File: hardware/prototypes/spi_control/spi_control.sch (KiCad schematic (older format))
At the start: 78 parts, among them J1 USB_B_Micro, J39 Versa_1, J40 Versa_2, U1 ST1L08SPU33R, U2 MCP2210-I_MQ, U3 ADAR7251, U4 BGT24_Module, Y1 12MHZ, Y2 40MHz

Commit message: Started routing SPI to USB. Started preliminary routing for the IQ data.
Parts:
- removed Y1: 12MHZ, Crystal:Crystal_SMD_Abracon_ABM8G-4Pin_3.2x2.5mm, symbol Device:Crystal
- removed Y2: 40MHz, Oscillator:Oscillator_SMD_Abracon_ASE-4Pin_3.2x2.5mm, symbol Device:Crystal
- added Y1: 12MHZ, Crystal:Crystal_SMD_Abracon_ABM8G-4Pin_3.2x2.5mm, symbol Device:Crystal_GND24
- added Y2: 40MHz, Oscillator:Oscillator_SMD_Abracon_ASE-4Pin_3.2x2.5mm, symbol Device:Crystal_GND24
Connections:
- net GND: now also Y1.2, Y1.4, Y2.2, Y2.4
- net PLL_MOD: now also J40.21 (Pin_21); no longer J40.25 (Pin_25)
- net PLL_RSET: now also J40.25 (Pin_25); no longer J40.21 (Pin_21)
- net USB_D+: now also D1.4; no longer D1.3
- net USB_D-: now also D1.3; no longer D1.4
- net at C21.2, U2.19 (OSC1): now also Y1.1
- net at C23.2, U2.20 (OSC2): now also Y1.3
- net at C26.2, R7.1: now also Y2.1
- net at C25.2, R6.1: now also Y2.3
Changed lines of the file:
@@
 $EndComp
 Wire Wire Line
-	1450 1500 1850 1500
-Wire Wire Line
-	2050 2000 1950 2000
-Wire Wire Line
-	1950 2000 1950 1600
-Wire Wire Line
 	1950 1600 1450 1600
 Wire Wire Line
-	2050 2200 1850 2200
-Wire Wire Line
-	1850 2200 1850 1500
-Wire Wire Line
 	2550 2000 2650 2000
 Wire Wire Line
@@
 Wire Wire Line
 	2850 2500 2850 2550
-$Comp
-L Device:Crystal Y1
-U 1 1 5DA6AEC7
-P 7500 2500
-F 0 "Y1" H 7500 2750 50  0000 C CNN
-F 1 "12MHZ" H 7500 2677 50  0000 C CNN
-F 2 "Crystal:Crystal_SMD_Abracon_ABM8G-4Pin_3.2x2.5mm" H 7500 2500 50  0001 C CNN
-F 3 "https://ecsxtal.com/store/pdf/ecx-32.pdf" H 7500 2500 50  0001 C CNN
-F 4 "ECS-120-12-33-AGN-TR" H 7500 2676 50  0001 C CNN "MPN"
-	1    7500 2500
-	1    0    0    -1
-$EndComp
 Wire Wire Line
 	7750 2250 7750 2500
@@
 	7250 2900 7250 2950
 Wire Wire Line
-	7250 2950 7500 2950
-Wire Wire Line
 	7750 2950 7750 2900
 $Comp
@@
 PLL Loop Filter
 $Comp
-L Device:Crystal Y2
-U 1 1 5DD040BC
-P 10700 8850
-F 0 "Y2" V 10746 8981 50  0000 L CNN
-F 1 "40MHz" V 10655 8981 50  0000 L CNN
-F 2 "Oscillator:Oscillator_SMD_Abracon_ASE-4Pin_3.2x2.5mm" H 10700 8850 50  0001 C CNN
-F 3 "https://ecsxtal.com/store/pdf/ecx-32.pdf" H 10700 8850 50  0001 C CNN
-F 4 "ECS-400-18-33-JGN-TR" V 10700 8850 50  0001 C CNN "MPN"
-	1    10700 8850
-	0    -1   -1   0
-$EndComp
-$Comp
 L Device:C C25
 U 1 1 5DD05357
@@
 $EndComp
 Wire Wire Line
-	10350 8600 10700 8600
-Wire Wire Line
-	10700 8700 10700 8600
-Connection ~ 10700 8600
-Wire Wire Line
-	10700 8600 10900 8600
-Wire Wire Line
 	11200 8600 11250 8600
 Wire Wire Line
@@
 	10900 9100 10700 9100
 Wire Wire Line
-	10700 9100 10700 9000
-Wire Wire Line
 	10700 9100 10350 9100
 Connection ~ 10700 9100
@@
 PLL_TRIG2
 Wire Wire Line
-	19250 5450 19250 6100
-Text Label 19250 6100 1    50   ~ 0
+	19050 5450 19050 6100
+Text Label 19050 6100 1    50   ~ 0
 PLL_MOD
 Wire Wire Line
@@
 PLL_MUX
 Wire Wire Line
-	19050 5450 19050 6100
-Text Label 19050 6100 1    50   ~ 0
+	19250 5450 19250 6100
+Text Label 19250 6100 1    50   ~ 0
 PLL_RSET
 Wire Wire Line
@@
 EndData
 $EndBitmap
+Wire Wire Line
+	1950 1600 1950 2200
+Wire Wire Line
+	1950 2200 2050 2200
+Wire Wire Line
+	2050 2000 2050 1500
+Wire Wire Line
+	1450 1500 2050 1500
+$Comp
+L Device:Crystal_GND24 Y1
+U 1 1 5FC6E4E6
+P 7500 2500
+F 0 "Y1" H 7694 2546 50  0000 L CNN
+F 1 "12MHZ" H 7375 2750 50  0000 L CNN
+F 2 "Crystal:Crystal_SMD_Abracon_ABM8G-4Pin_3.2x2.5mm" H 7500 2500 50  0001 C CNN
+F 3 "https://ecsxtal.com/store/pdf/ecx-32.pdf" H 7500 2500 50  0001 C CNN
+F 4 "ECS-120-12-33-AGN-TR" H 7500 2500 50  0001 C CNN "MPN"
+	1    7500 2500
+	1    0    0    -1
+$EndComp
+Connection ~ 10700 8600
+Wire Wire Line
+	10700 8600 10900 8600
+Wire Wire Line
+	10350 8600 10700 8600
+Wire Wire Line
+	10700 8600 10700 8725
+Wire Wire Line
+	10700 9100 10700 9025
+Wire Wire Line
+	7250 2950 7500 2950
+Wire Wire Line
+	7500 2950 7500 2700
+Wire Wire Line
+	7500 2300 7500 2200
+Wire Wire Line
+	7500 2200 7675 2200
+$Comp
+L power:GND #PWR0146
+U 1 1 60004941
+P 7675 2350
+F 0 "#PWR0146" H 7675 2100 50  0001 C CNN
+F 1 "GND" H 7600 2375 50  0000 C CNN
+F 2 "" H 7675 2350 50  0001 C CNN
+F 3 "" H 7675 2350 50  0001 C CNN
+	1    7675 2350
+	1    0    0    -1
+$EndComp
+Wire Wire Line
+	7675 2200 7675 2350
+$Comp
+L power:GND #PWR0147
+U 1 1 600397BF
+P 10950 8875
+F 0 "#PWR0147" H 10950 8625 50  0001 C CNN
+F 1 "GND" H 10955 8702 50  0000 C CNN
+F 2 "" H 10950 8875 50  0001 C CNN
+F 3 "" H 10950 8875 50  0001 C CNN
+	1    10950 8875
+	1    0    0    -1
+$EndComp
+$Comp
+L Device:Crystal_GND24 Y2
+U 1 1 5FD6D80E
+P 10700 8875
+F 0 "Y2" H 10850 9125 50  0000 L CNN
+F 1 "40MHz" H 10575 9125 50  0000 L CNN
+F 2 "Oscillator:Oscillator_SMD_Abracon_ASE-4Pin_3.2x2.5mm" H 10700 8875 50  0001 C CNN
+F 3 "https://ecsxtal.com/store/pdf/ecx-32.pdf" H 10700 8875 50  0001 C CNN
+F 4 "ECS-400-18-33-JGN-TR" H 10700 8875 50  0001 C CNN "MPN"
+	1    10700 8875
+	0    -1   -1   0
+$EndComp
+Wire Wire Line
+	10900 8875 10950 8875
+$Comp
+L power:GND #PWR0148
+U 1 1 6017CD63
+P 10450 8875
+F 0 "#PWR0148" H 10450 8625 50  0001 C CNN
+F 1 "GND" H 10455 8702 50  0000 C CNN
+F 2 "" H 10450 8875 50  0001 C CNN
+F 3 "" H 10450 8875 50  0001 C CNN
+	1    10450 8875
+	-1   0    0    -1
+$EndComp
+Wire Wire Line
+	10500 8875 10450 8875
 $EndSCHEMATC

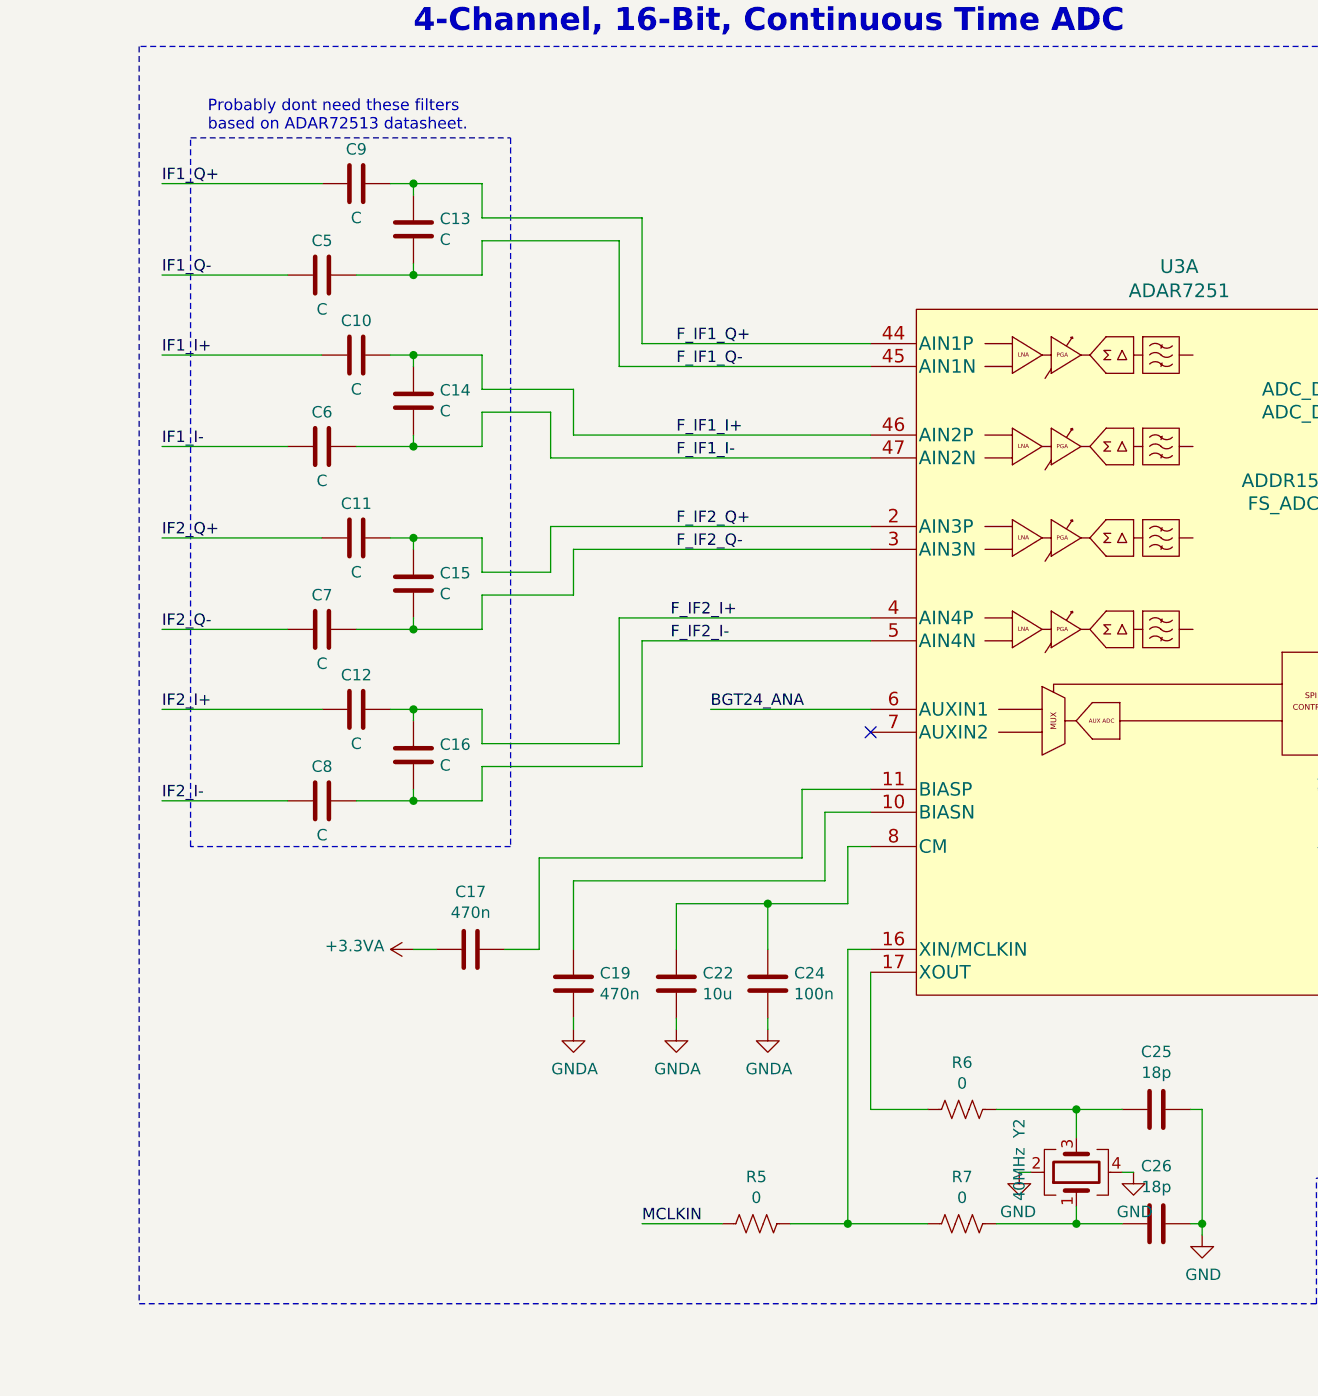
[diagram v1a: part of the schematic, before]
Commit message: Completed power section, completed analog power and gnd plane,fixed IQ lines to be symmetric, ADC 80% routing completed.
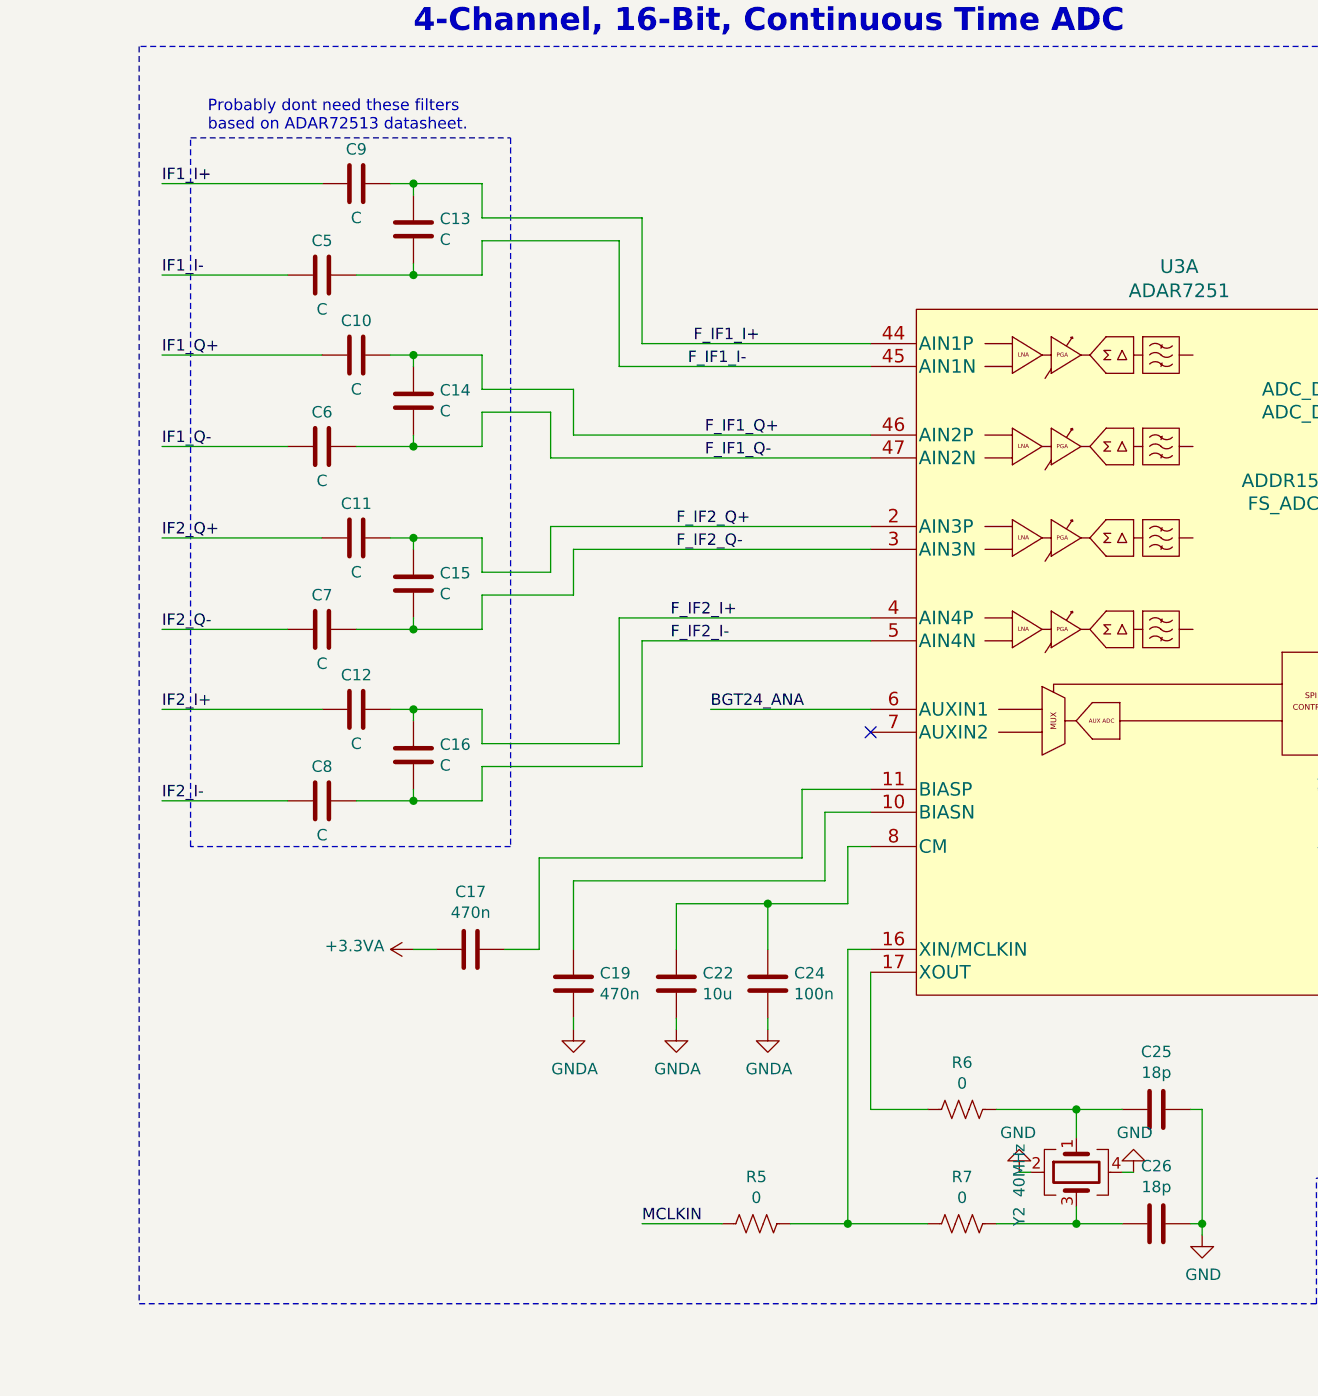
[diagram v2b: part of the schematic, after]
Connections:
- net F_IF1_I+: now also C13.2, C9.2, U3.44 (AIN1P); no longer C10.2, C14.2, U3.46 (AIN2P)
- net F_IF1_I-: now also C13.1, C5.2, U3.45 (AIN1N); no longer C14.1, C6.2, U3.47 (AIN2N)
- net F_IF1_Q+: now also C10.2, C14.2, U3.46 (AIN2P); no longer C13.2, C9.2, U3.44 (AIN1P)
- net F_IF1_Q-: now also C14.1, C6.2, U3.47 (AIN2N); no longer C13.1, C5.2, U3.45 (AIN1N)
- net IF1_I+: now also C9.1; no longer C10.1
- net IF1_I-: now also C5.1; no longer C6.1
- net IF1_Q+: now also C10.1; no longer C9.1
- net IF1_Q-: now also C6.1; no longer C5.1
- net at C25.2, R6.1: now also Y2.1; no longer Y2.3
- net at C26.2, R7.1: now also Y2.3; no longer Y2.1
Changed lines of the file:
@@
 Text Label 18625 8425 1    50   ~ 0
 PLL_DIV_MCU
-Text Label 8925 6550 0    50   ~ 0
-F_IF2_I-
-Text Label 8925 6450 0    50   ~ 0
-F_IF2_I+
-Text Label 8950 6150 0    50   ~ 0
-F_IF2_Q-
-Text Label 8950 6050 0    50   ~ 0
-F_IF2_Q+
-Text Label 8950 5750 0    50   ~ 0
+Text Label 9000 5350 0    50   ~ 0
 F_IF1_I-
-Text Label 8950 5650 0    50   ~ 0
+Text Label 9025 5250 0    50   ~ 0
 F_IF1_I+
-Text Label 8950 5350 0    50   ~ 0
+Text Label 9075 5750 0    50   ~ 0
 F_IF1_Q-
-Text Label 8950 5250 0    50   ~ 0
+Text Label 9075 5650 0    50   ~ 0
 F_IF1_Q+
-Text Label 6700 4550 0    50   ~ 0
+Text Label 6700 5300 0    50   ~ 0
 IF1_Q+
 Wire Notes Line
@@
 Wire Wire Line
 	6700 4550 7400 4550
-Text Label 6700 5700 0    50   ~ 0
+Text Label 6700 4950 0    50   ~ 0
 IF1_I-
-Text Label 6700 5300 0    50   ~ 0
+Text Label 6700 4550 0    50   ~ 0
 IF1_I+
-Text Label 6700 4950 0    50   ~ 0
+Text Label 6700 5700 0    50   ~ 0
 IF1_Q-
 Wire Wire Line
@@
 Wire Wire Line
 	6700 6100 7400 6100
-Text Label 6700 7250 0    50   ~ 0
-IF2_I-
-Text Label 6700 6850 0    50   ~ 0
-IF2_I+
-Text Label 6700 6500 0    50   ~ 0
-IF2_Q-
-Text Label 6700 6100 0    50   ~ 0
-IF2_Q+
 Wire Wire Line
 	18525 7275 18525 6625
@@
 F 3 "" H 10950 8875 50  0001 C CNN
 	1    10950 8875
-	1    0    0    -1
+	1    0    0    1
 $EndComp
 $Comp
@@
 F 4 "ECS-400-18-33-JGN-TR" H 10700 8875 50  0001 C CNN "MPN"
 	1    10700 8875
-	0    -1   -1   0
+	0    -1   1    0
 $EndComp
 Wire Wire Line
@@
 F 3 "" H 10450 8875 50  0001 C CNN
 	1    10450 8875
-	-1   0    0    -1
+	-1   0    0    1
 $EndComp
 Wire Wire Line
 	10500 8875 10450 8875
+Text Label 8950 6150 0    50   ~ 0
+F_IF2_Q-
+Text Label 8925 6550 0    50   ~ 0
+F_IF2_I-
+Text Label 8950 6050 0    50   ~ 0
+F_IF2_Q+
+Text Label 8925 6450 0    50   ~ 0
+F_IF2_I+
+Text Label 6700 6500 0    50   ~ 0
+IF2_Q-
+Text Label 6700 7250 0    50   ~ 0
+IF2_I-
+Text Label 6700 6850 0    50   ~ 0
+IF2_I+
+Text Label 6700 6100 0    50   ~ 0
+IF2_Q+
 $EndSCHEMATC

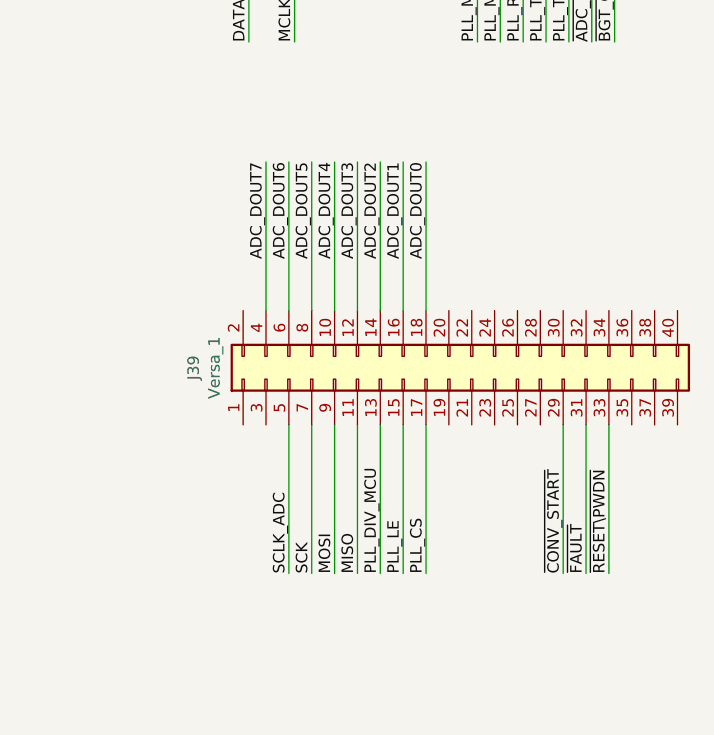
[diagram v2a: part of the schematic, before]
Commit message: Finished, DRC approved,  All nets routed.
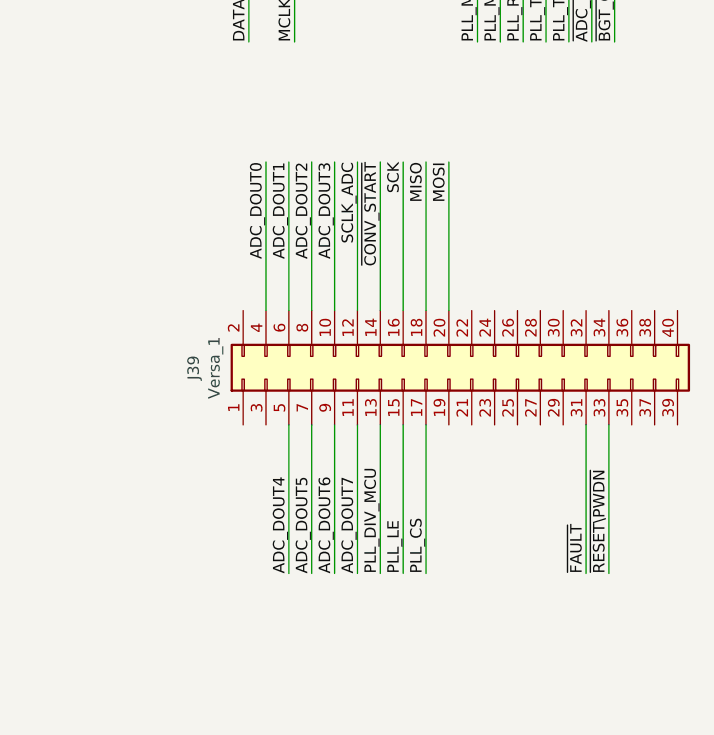
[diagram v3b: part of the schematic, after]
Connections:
- net ADC_DOUT0: now also J39.4 (Pin_4); no longer J39.18 (Pin_18)
- net ADC_DOUT1: now also J39.6 (Pin_6); no longer J39.16 (Pin_16)
- net ADC_DOUT2: now also J39.8 (Pin_8); no longer J39.14 (Pin_14)
- net ADC_DOUT3: now also J39.10 (Pin_10); no longer J39.12 (Pin_12)
- net ADC_DOUT4: now also J39.5 (Pin_5); no longer J39.10 (Pin_10)
- net ADC_DOUT5: now also J39.7 (Pin_7); no longer J39.8 (Pin_8)
- net ADC_DOUT6: now also J39.9 (Pin_9); no longer J39.6 (Pin_6)
- net ADC_DOUT7: now also J39.11 (Pin_11); no longer J39.4 (Pin_4)
- net MISO: now also J39.18 (Pin_18); no longer J39.11 (Pin_11)
- net MOSI: now also J39.20 (Pin_20); no longer J39.9 (Pin_9)
- net SCK: now also J39.16 (Pin_16); no longer J39.7 (Pin_7)
- net SCLK_ADC: now also J39.12 (Pin_12); no longer J39.5 (Pin_5)
- net ~CONV_START: now also J39.14 (Pin_14); no longer J39.29 (Pin_29)
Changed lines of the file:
@@
 $EndComp
 Wire Wire Line
-	19425 7775 19425 8425
+	18625 7275 18625 6625
 Wire Wire Line
 	19625 7775 19625 8425
 Wire Wire Line
 	19525 7775 19525 8425
-Text Label 19425 8425 1    50   ~ 0
+Text Label 18625 6625 3    50   ~ 0
 ~CONV_START
 Text Label 18050 6100 1    50   ~ 0
@@
 	19550 5450 19550 6100
 Wire Wire Line
-	18325 7775 18325 8425
-Wire Wire Line
-	18425 7775 18425 8425
-Wire Wire Line
-	18525 7775 18525 8425
+	18725 7275 18725 6625
+Wire Wire Line
+	18925 7275 18925 6625
+Wire Wire Line
+	18825 7275 18825 6625
 Wire Wire Line
 	18825 7775 18825 8425
 Wire Wire Line
 	19650 5450 19650 6100
-Text Label 18525 8425 1    50   ~ 0
+Text Label 18825 6625 3    50   ~ 0
 MISO
-Text Label 18425 8425 1    50   ~ 0
+Text Label 18925 6625 3    50   ~ 0
 MOSI
-Text Label 18325 8425 1    50   ~ 0
+Text Label 18725 6625 3    50   ~ 0
 SCK
 Text Label 18825 8425 1    50   ~ 0
@@
 	6700 6100 7400 6100
 Wire Wire Line
+	18425 7275 18425 6625
+Wire Wire Line
+	18325 7275 18325 6625
+Wire Wire Line
+	18225 7275 18225 6625
+Wire Wire Line
+	18125 7275 18125 6625
+Text Label 18525 6625 3    50   ~ 0
+SCLK_ADC
+Text Label 18525 8425 1    50   ~ 0
+ADC_DOUT7
+Text Label 18425 8425 1    50   ~ 0
+ADC_DOUT6
+Text Label 18325 8425 1    50   ~ 0
+ADC_DOUT5
+Text Label 18225 8425 1    50   ~ 0
+ADC_DOUT4
+Text Label 18425 6625 3    50   ~ 0
+ADC_DOUT3
+Text Label 18325 6625 3    50   ~ 0
+ADC_DOUT2
+Text Label 18225 6625 3    50   ~ 0
+ADC_DOUT1
+Text Label 18125 6625 3    50   ~ 0
+ADC_DOUT0
+Wire Wire Line
 	18525 7275 18525 6625
 Wire Wire Line
-	18625 7275 18625 6625
-Wire Wire Line
-	18725 7275 18725 6625
-Wire Wire Line
-	18825 7275 18825 6625
-Text Label 18225 8425 1    50   ~ 0
-SCLK_ADC
-Text Label 18125 6625 3    50   ~ 0
-ADC_DOUT7
-Text Label 18225 6625 3    50   ~ 0
-ADC_DOUT6
-Text Label 18325 6625 3    50   ~ 0
-ADC_DOUT5
-Text Label 18425 6625 3    50   ~ 0
-ADC_DOUT4
-Text Label 18525 6625 3    50   ~ 0
-ADC_DOUT3
-Text Label 18625 6625 3    50   ~ 0
-ADC_DOUT2
-Text Label 18725 6625 3    50   ~ 0
-ADC_DOUT1
-Text Label 18825 6625 3    50   ~ 0
-ADC_DOUT0
+	18525 7775 18525 8425
+Wire Wire Line
+	18425 7775 18425 8425
+Wire Wire Line
+	18325 7775 18325 8425
 Wire Wire Line
 	18225 7775 18225 8425
 Wire Wire Line
-	18125 7275 18125 6625
-Wire Wire Line
-	18225 7275 18225 6625
-Wire Wire Line
-	18325 7275 18325 6625
-Wire Wire Line
-	18425 7275 18425 6625
-Wire Wire Line
 	18725 7775 18725 8425

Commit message: Added 3d model for ADAR7251 and moved footprint into bloop.pretty. Updated schematic, J39-13 swaped with J39-15. Corrected stackup text in layout to ECO1 layer from BCu.
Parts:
- U3: footprint Package_CSP:LFCSP-48-1EP_7x7mm_P0.5mm_EP4.1x4.1mm_ThermalVias -> bloop:LFCSP-48-1EP_7x7mm_P0.5mm_EP4.1x4.1mm
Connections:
- net PLL_DIV_MCU: now also J39.15 (Pin_15); no longer J39.13 (Pin_13)
- net PLL_LE: now also J39.13 (Pin_13); no longer J39.15 (Pin_15)
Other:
- note added: "Output Connectors"
- note added: "RF Transceiver - BGT24 Module"
- note removed: "Output Connector"
- moved on the sheet: C10, C11, C12, C13, C14, C15, C16, C17, C19, C22, C24, C25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
